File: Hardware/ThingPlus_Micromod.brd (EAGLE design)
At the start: 91.4 x 22.9 mm, 70 parts, among them J4 QWIIC_RIGHT_ANGLE, J5 MICRO-SD-SDIOPUSH-PUSH, J6 JTAG, J7 MICROMOD-2222-C, U2 MCP73831, U3 MAX17048, U4 3.3V, U6 AP7361C-33

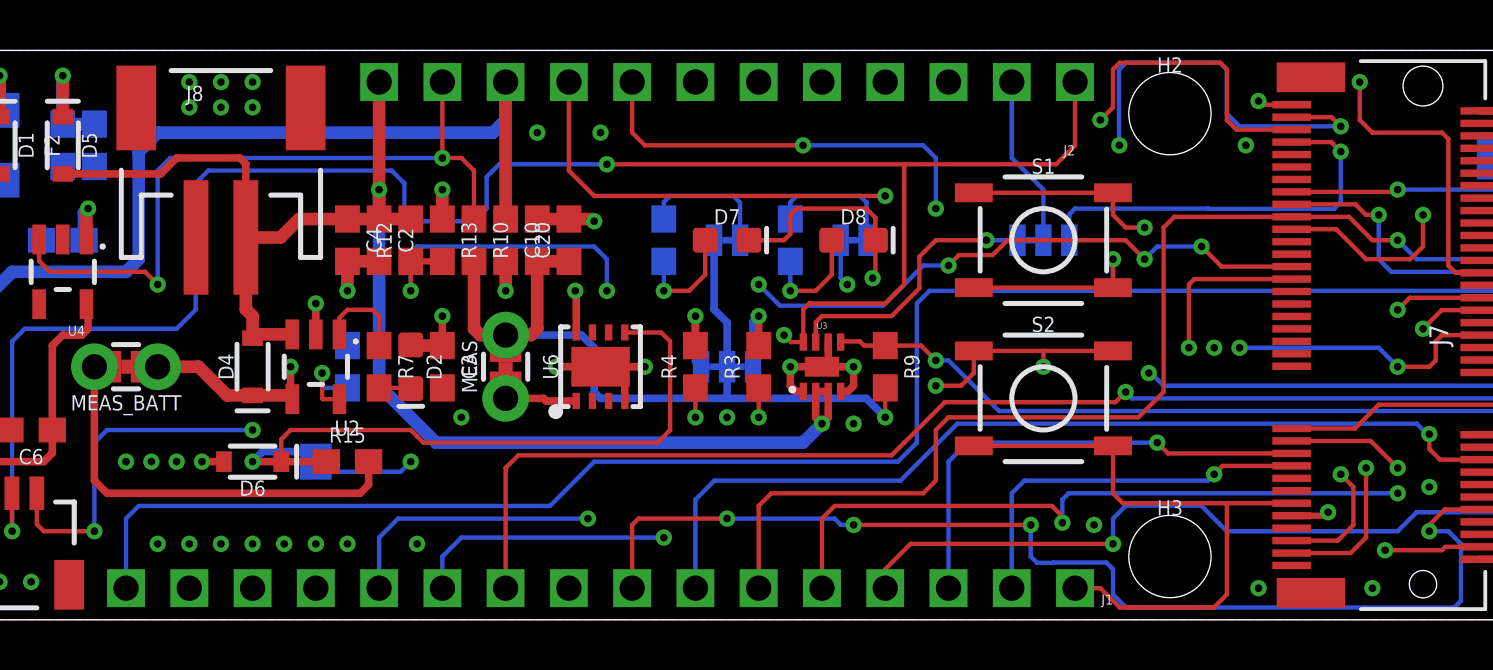
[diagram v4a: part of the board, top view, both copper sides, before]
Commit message: Rename SCL/G7 net to SCL.
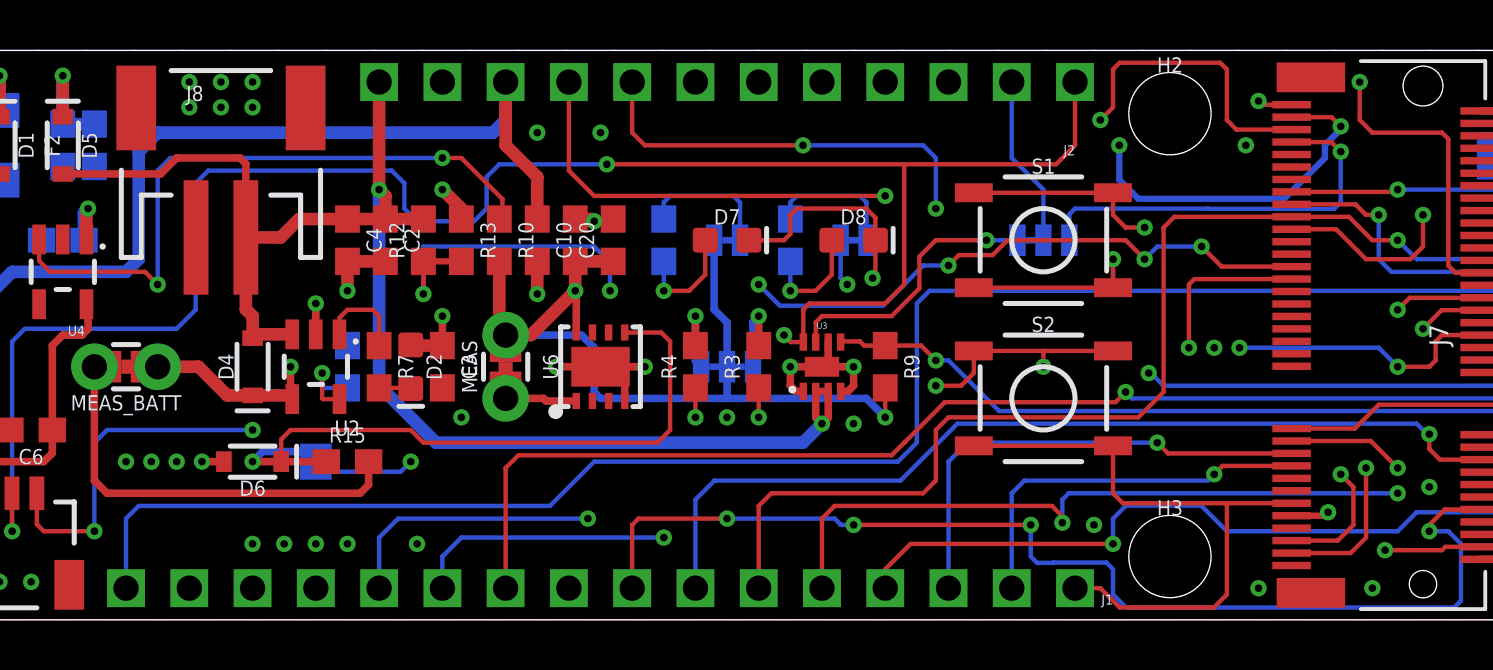
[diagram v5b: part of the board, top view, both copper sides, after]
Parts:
- moved C20 1.78 mm to (33.5, 15.2)
- moved C21 1.52 mm to (32.0, 15.2)
- moved C10 1.27 mm to (30.5, 15.2)
- moved R10 1.02 mm to (29.0, 15.2)
- moved R13 0.76 mm to (27.4, 15.2)
- moved R12 0.51 mm to (25.9, 15.2)
- moved C2 0.25 mm to (24.4, 15.2)
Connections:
- removed net EN: J2.11, R10.1, U4.3
- removed net SCL/G7: J4.4, R3.1
- new net QWIIC_EN: J7.67, R10.1, U4.3
- net 3.3V_EN: now also J2.11
- net SCL: now also J4.4, R3.1
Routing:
- net SCL: track 43.5 -> 79.9 mm, vias 2 -> 5
- net SCL/G7: track 36.4 -> 0.00 mm, vias 3 -> 0
- net EN: track 28.7 -> 0.00 mm, vias 2 -> 0
- net QWIIC_EN: track 0.00 -> 26.1 mm, vias 0 -> 2
- net G5: track 27.6 -> 25.7 mm
- net GND: track 54.3 -> 53.5 mm, vias 56 -> 53
- net V_BATT: track 59.1 -> 59.7 mm
- net V_USB: track 111.2 -> 111.8 mm

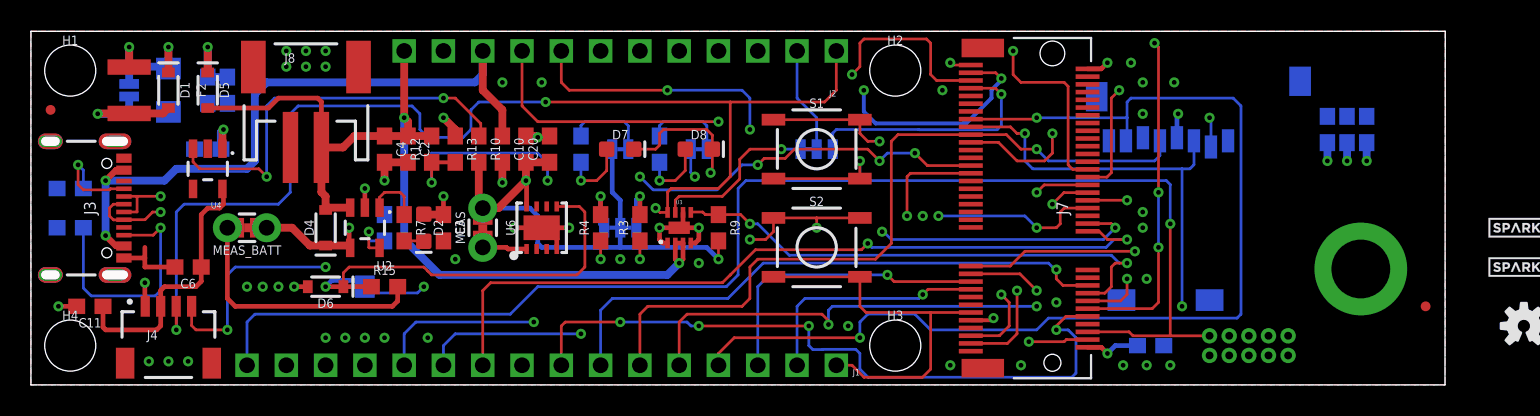
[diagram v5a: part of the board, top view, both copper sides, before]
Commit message: Moved components to remove clearance errors; optimized GND and VCC polygons; fixed schematic off-grid components and fixed CamelCasing. TODO: add labels.
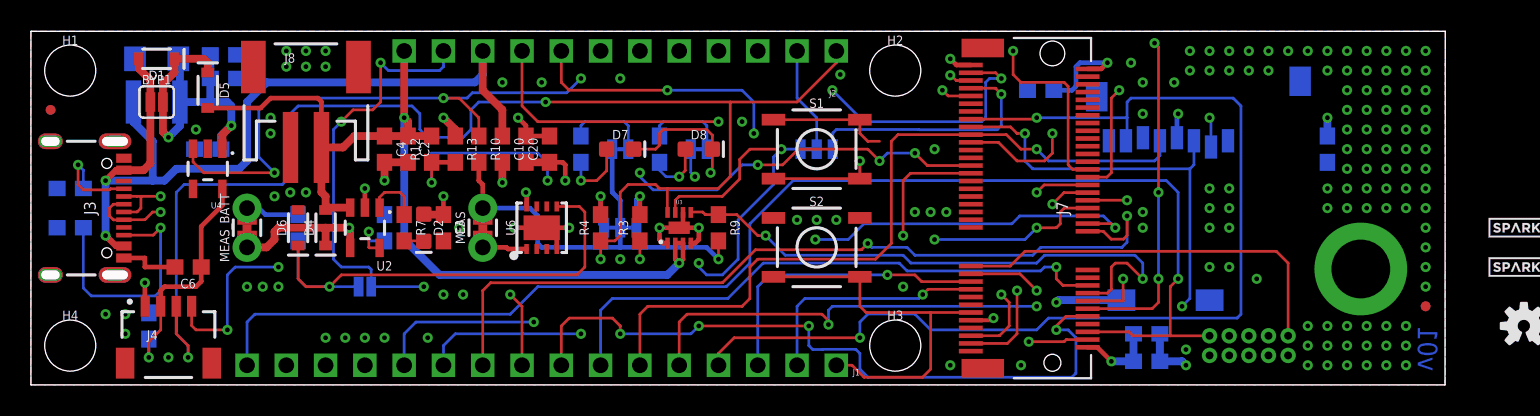
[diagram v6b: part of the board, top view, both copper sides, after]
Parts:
- added FD2, FD3: FIDUCIALUFIDUCIAL, SparkFun-Aesthetics:FIDUCIAL-MICRO
- moved FRAME1 36.1 mm to (23.1, 23.9)
- moved C13 20.7 mm to (72.1, 1.52), turned to 180 degrees
- moved C8 18.7 mm to (65.3, 19.1), turned to 180 degrees
- moved R15 6.76 mm to (17.3, 10.2), flipped to the bottom, turned to 90 degrees
- moved D6 4.20 mm to (17.3, 10.2), turned to 90 degrees
- moved C11 4.02 mm to (7.62, 3.81), flipped to the bottom, turned to 90 degrees
- moved C18 2.50 mm to (12.4, 21.3), turned to 180 degrees
- moved C19 2.17 mm to (8.13, 21.1), turned to 180 degrees
- moved D1 2.17 mm to (8.13, 21.1), turned to 180 degrees
- moved BYP1 1.93 mm to (8.13, 18.3), flipped to the top, turned to 0 degrees
- moved F2 1.93 mm to (8.13, 18.3), flipped to the bottom, turned to 180 degrees
- moved C7 1.80 mm to (83.8, 15.2), turned to 90 degrees
- moved C22 0.80 mm to (72.1, 3.30)
- moved C17 0.80 mm to (12.4, 19.8), turned to 180 degrees
- turned MEAS_BATT to 90 degrees
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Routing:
- net QWIIC_EN: track 26.1 -> 64.8 mm, vias 2 -> 4
- net 3.3V_EN: track 49.9 -> 73.9 mm, vias 2 -> 4
- net SCL: track 79.9 -> 95.9 mm, vias 5 -> 6
- net V_USB: track 111.8 -> 120.6 mm, vias 4 -> 3
- net A1: track 55.6 -> 49.6 mm
- net VIN: track 72.5 -> 67.1 mm, vias 6 -> 4
- net 3.3V_EN_VE: track 28.3 -> 33.5 mm
- net !I2C_INT!: track 33.7 -> 37.7 mm
- net SDA: track 126.1 -> 129.7 mm, vias 7 -> 6
- net PWM0: track 50.8 -> 54.2 mm
- net 5V: track 18.3 -> 21.0 mm
- net QWIIC_PWR: track 17.5 -> 15.2 mm, vias 0 -> 1
- net 3.3V: track 45.8 -> 47.2 mm, vias 7 -> 6
- net GND: track 53.5 -> 52.1 mm, vias 53 -> 154
- net PWM1: track 40.6 -> 41.9 mm, vias 2 -> 3
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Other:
- board text added: "Ricardo R."
- board text added: "v01"

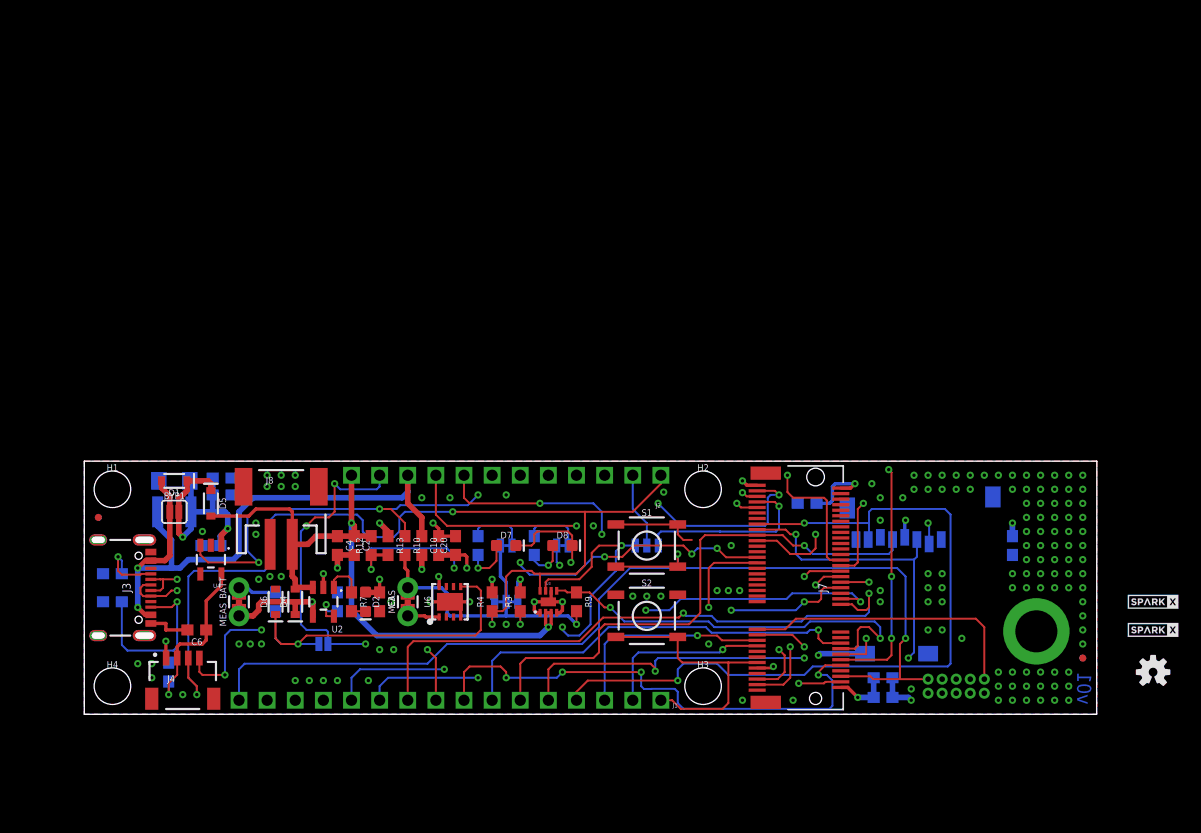
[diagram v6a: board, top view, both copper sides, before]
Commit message: Added buzzard labels to ThingPlus MicroMod
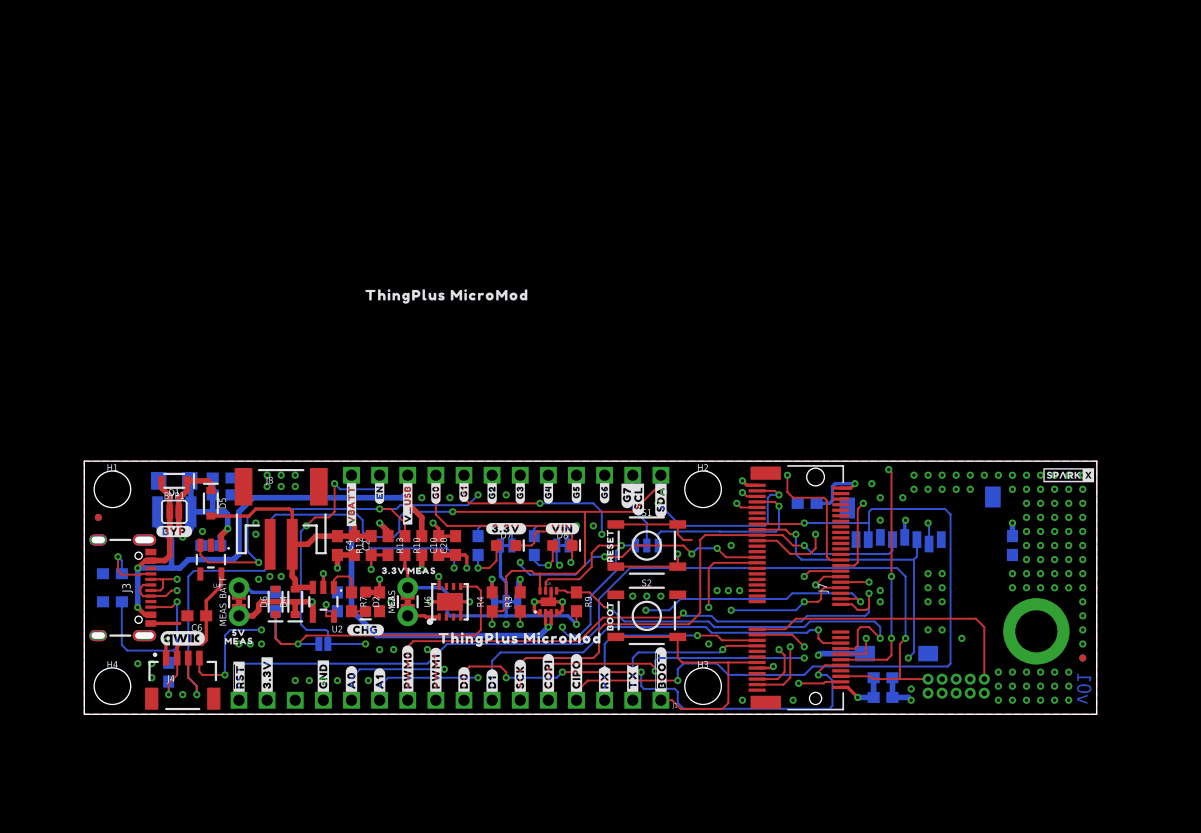
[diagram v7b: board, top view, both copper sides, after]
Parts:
- added LOGO2, LOGO3: QWIIC_LOGO_4MM, SparkFun-Aesthetics:QWIIC_4MM
- added U$10, U$74: (no value), output:3#3V18
- added U$11, U$14, U$75, U$77: (no value), output:MEAS18
- added U$12: (no value), output:#CHG#18
- added U$13, U$76: (no value), output:5V18
- added U$15, U$48: (no value), output:#D0#5
- added U$16, U$49: (no value), output:#D1#5
- added U$17, U$50: (no value), output:#SCK#5
- added U$18, U$51: (no value), output:#COPI#6
- added U$19, U$52: (no value), output:#CIPO#7
- added U$20, U$53: (no value), output:#RX#8
- added U$21, U$54: (no value), output:#TX#9
- added U$22, U$55: (no value), output:##BOOT##10
- added U$23: (no value), output:BOOT14
- added U$24: (no value), output:RESET15
- added U$25, U$56: (no value), output:#VBATT#13
- added U$26, U$57: (no value), output:#EN#13
- added U$27, U$58: (no value), output:#V_USB#12
- added U$28, U$59: (no value), output:#G0#12
- added U$29, U$60: (no value), output:#G1#12
- added U$3, U$41: (no value), output:##RST##0
- added U$30, U$61: (no value), output:#G2#12
- added U$31, U$62: (no value), output:#G3#12
- added U$32, U$63: (no value), output:#G4#12
- added U$33, U$64: (no value), output:#G5#12
- added U$34, U$65: (no value), output:#G6#12
- added U$35, U$66: (no value), output:#SDA#11
- added U$36, U$67: (no value), output:#G7#13
- added U$37, U$68: (no value), output:#SCL#12
- added U$38, U$72: (no value), output:#VIN#21
- added U$39, U$71: (no value), output:#3#3V#21
- added U$4, U$42: (no value), output:#3#3V#1
- added U$40: (no value), output:#BYP#24
- added U$43, U$5: (no value), output:#GND#4
- added U$44, U$6: (no value), output:#A0#5
- added U$45, U$7: (no value), output:#A1#5
- added U$46, U$8: (no value), output:#PWM0#5
- added U$47, U$9: (no value), output:#PWM1#5
- added U$69, U$79, U$80: (no value), output:THINGPLUS_MICROMOD25
- added U$70: (no value), output:#3#3V_EN#22
- added U$73: (no value), output:#I2C#23
- added U$78: (no value), output:#SCL#G7#23
- U$2: value SPARKX-LOGO2 -> SPARKX-LOGO4; device SparkX:SPARKX-TINY -> SparkX:SPARKX-MEDIUM
- U4: device SparkFun-IC-Power:SOT23-5@1 -> SparkFun-IC-Power:SOT23-5
- moved U$2 45.7 mm to (50.8, 8.89), flipped to the bottom
- moved U$1 13.7 mm to (88.9, 21.6)
- moved LOGO1 7.73 mm to (88.9, 2.54), flipped to the bottom
- moved C6 1.27 mm to (10.2, 8.89)
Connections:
- net !RESET! renamed !RST!
- net 3.3V_EN renamed EN
- net N$5 renamed SCL/G7
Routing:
- net GND: track 52.1 -> 50.8 mm
